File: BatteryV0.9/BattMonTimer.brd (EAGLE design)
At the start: 88 x 88 mm, 62 parts, among them IC1 TMP36GT9Z, IC2 TLV2211, IC3 INA138, IC4 TMP36GRT, IC6 CD74HC4060, IC7 74LVC1G74DCT, IC8 ICM7555SO08, M1 Mount, M2 Mount, P2 SSM3J338RSOT-23F_TOS-M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

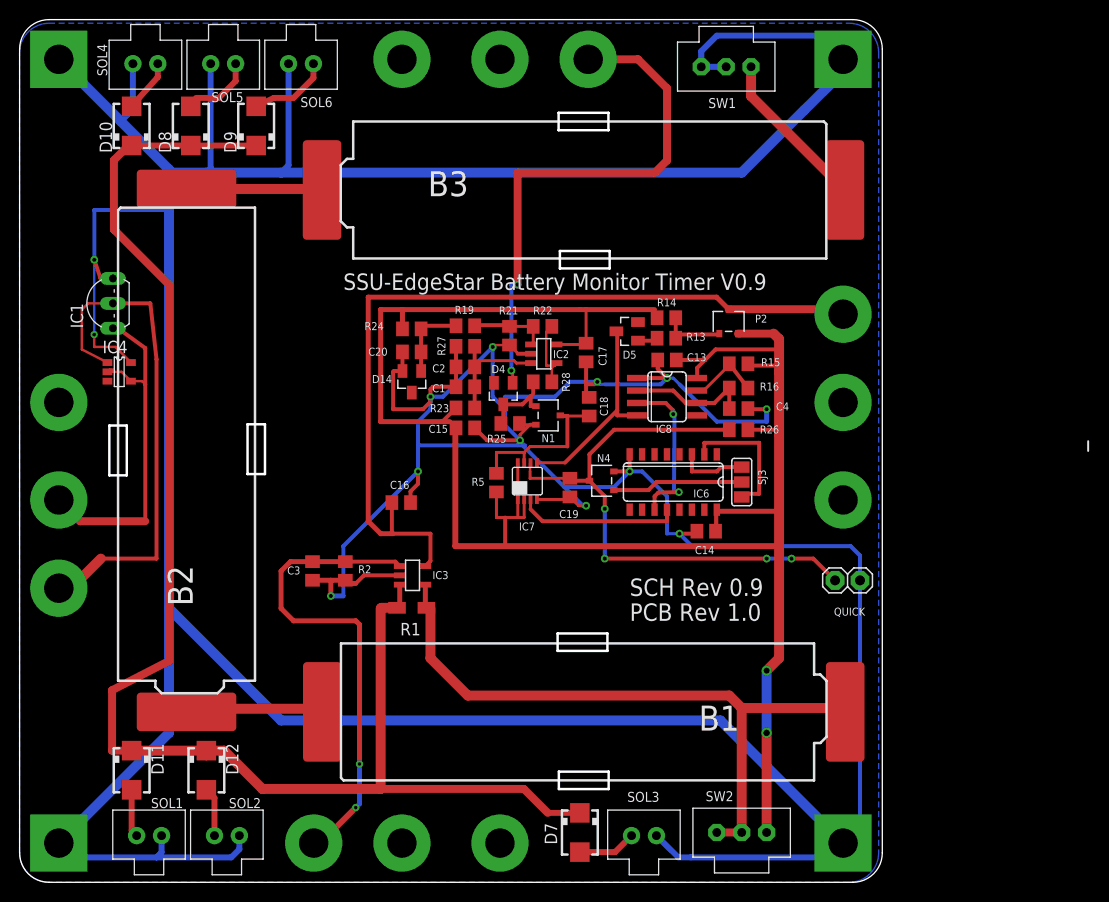
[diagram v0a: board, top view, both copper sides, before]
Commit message: 
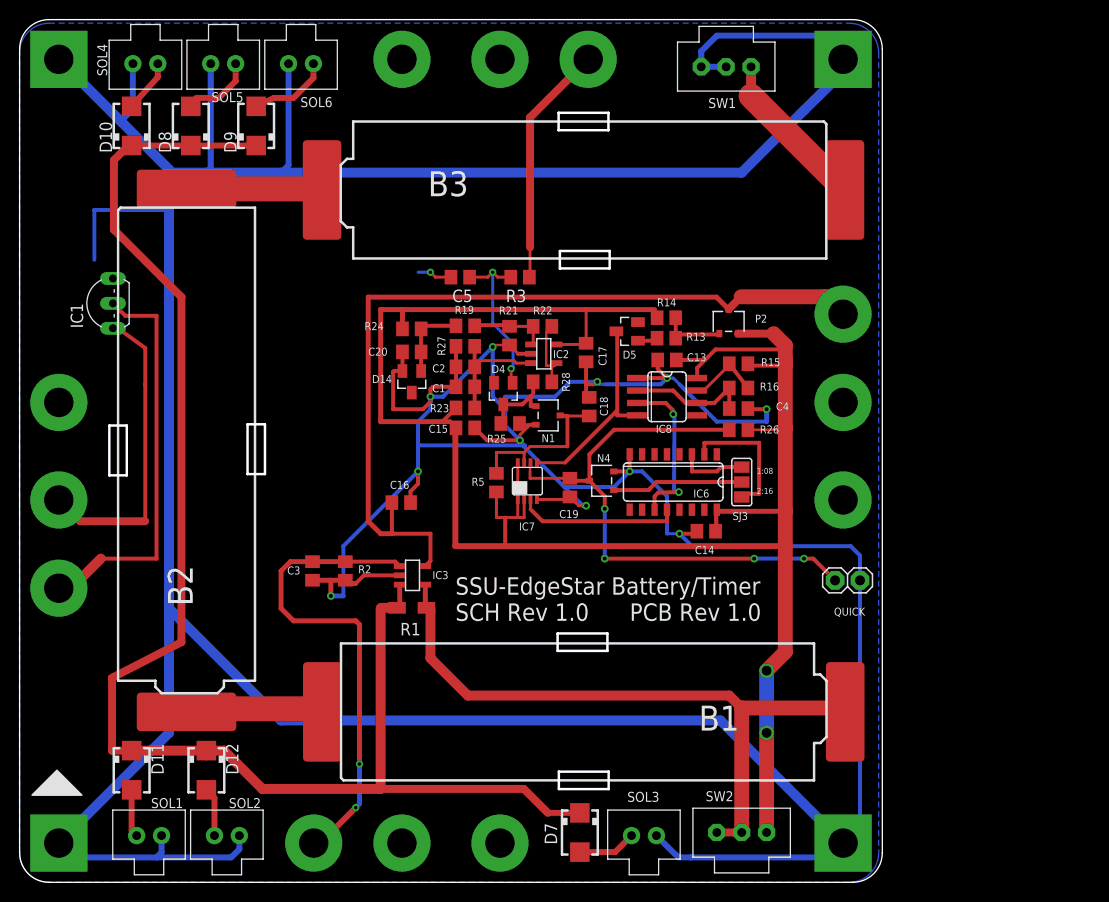
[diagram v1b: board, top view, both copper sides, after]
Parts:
- removed IC4: TMP36GRT, BattMonTimer:SOT-23-5
- added C5: 10 uf, rcl:C0805
- added R3: 120, rcl:R0805
- C1: value 10 uf ,XR7 -> 10u
- C2: value Spare,XR7 -> (none)
- R1: value 1o -> 1.0o
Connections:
- net N$38 renamed V_OUT
- net SOL_CURRENT renamed SOL_I
- removed net N$2: IC1.2, IC4.1, M2.P$3
- removed net N$3: IC1.1, IC4.2, IC4.4, M2.P$4, M2.P$7
- new net BATT_TEMP: IC1.2, M2.P$3
- new net N$5: C5.1, D4.1, R3.2
- new net SYS_V3_3: IC1.1, M2.P$4, M2.P$7
- net GND: now also C5.2; no longer IC4.5
- net UVP_TRIG: now also R3.1; no longer D4.1
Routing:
- net N$2: track 51.5 -> 0.00 mm
- net BATT_TEMP: track 0.00 -> 40.9 mm
- net N$3: track 36.4 -> 0.00 mm
- net SYS_V3_3: track 0.00 -> 31.3 mm
- net UVP_TRIG: track 54.5 -> 24.7 mm, vias 2 -> 0
- net N$5: track 0.00 -> 16.9 mm, vias 0 -> 2
- net GND: track 598.7 -> 585.7 mm, vias 13 -> 12
- net V-BATTTERY+: track 207.1 -> 209.8 mm
- net N$4: track 155.2 -> 156.5 mm
- net V_OUT: track 85.6 -> 86.7 mm
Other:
- board text added: "1:08"
- board text added: "2:16"
- board text added: "SCH Rev 1.0"
- board text added: "SSU-EdgeStar Battery/Timer"
- board text removed: "SCH Rev 0.9"
- board text removed: "SSU-EdgeStar Battery Monitor Timer V0.9"
